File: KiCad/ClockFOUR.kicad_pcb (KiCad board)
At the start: 2 copper layers, 210 x 228 mm, 406 parts, among them P1 ICSP, P2 FTDI, P3 LDR_header, P4 Button_Header, P5 BARREL_JACK, SW1 SW_RST, U1 ATMEGA328P, U2 DS3231N, X1 CRYSTAL

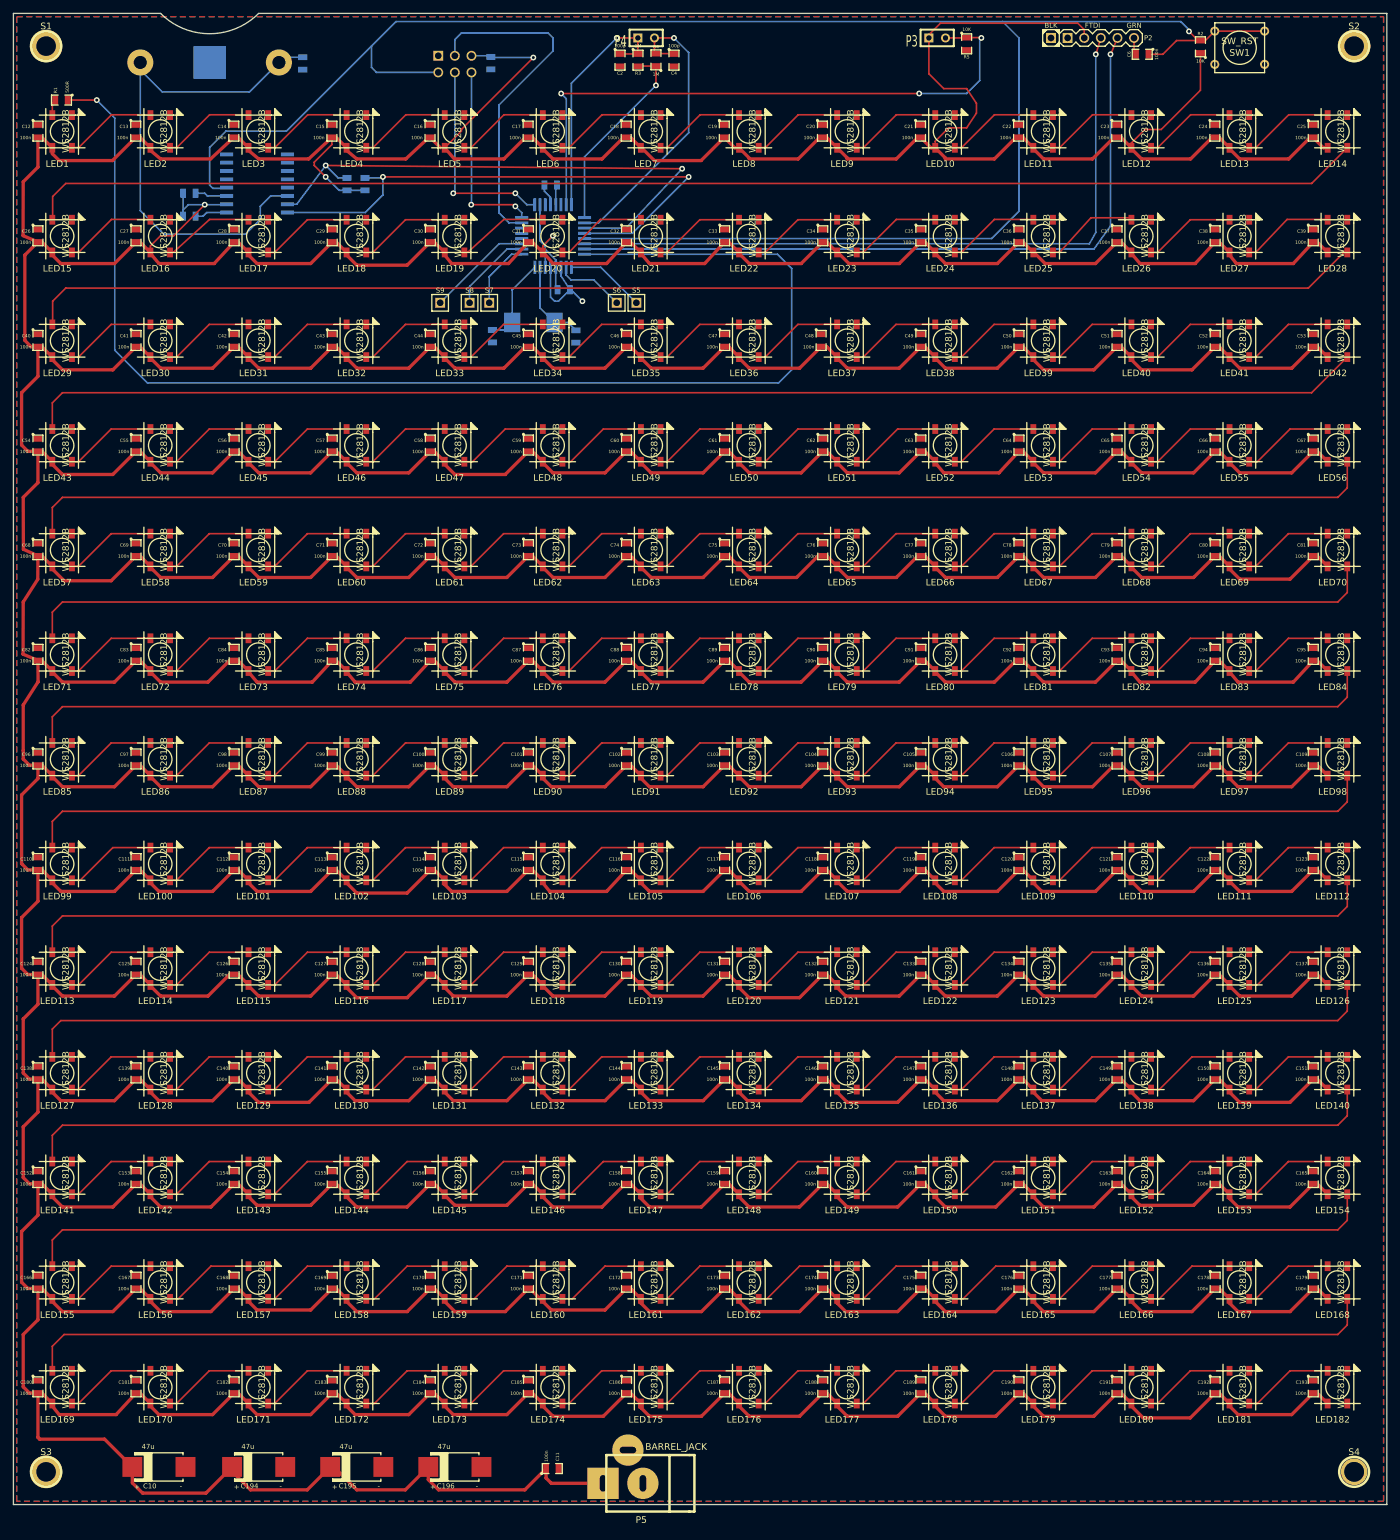
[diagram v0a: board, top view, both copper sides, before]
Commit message: Connector nudged, sent to Seed for quotation
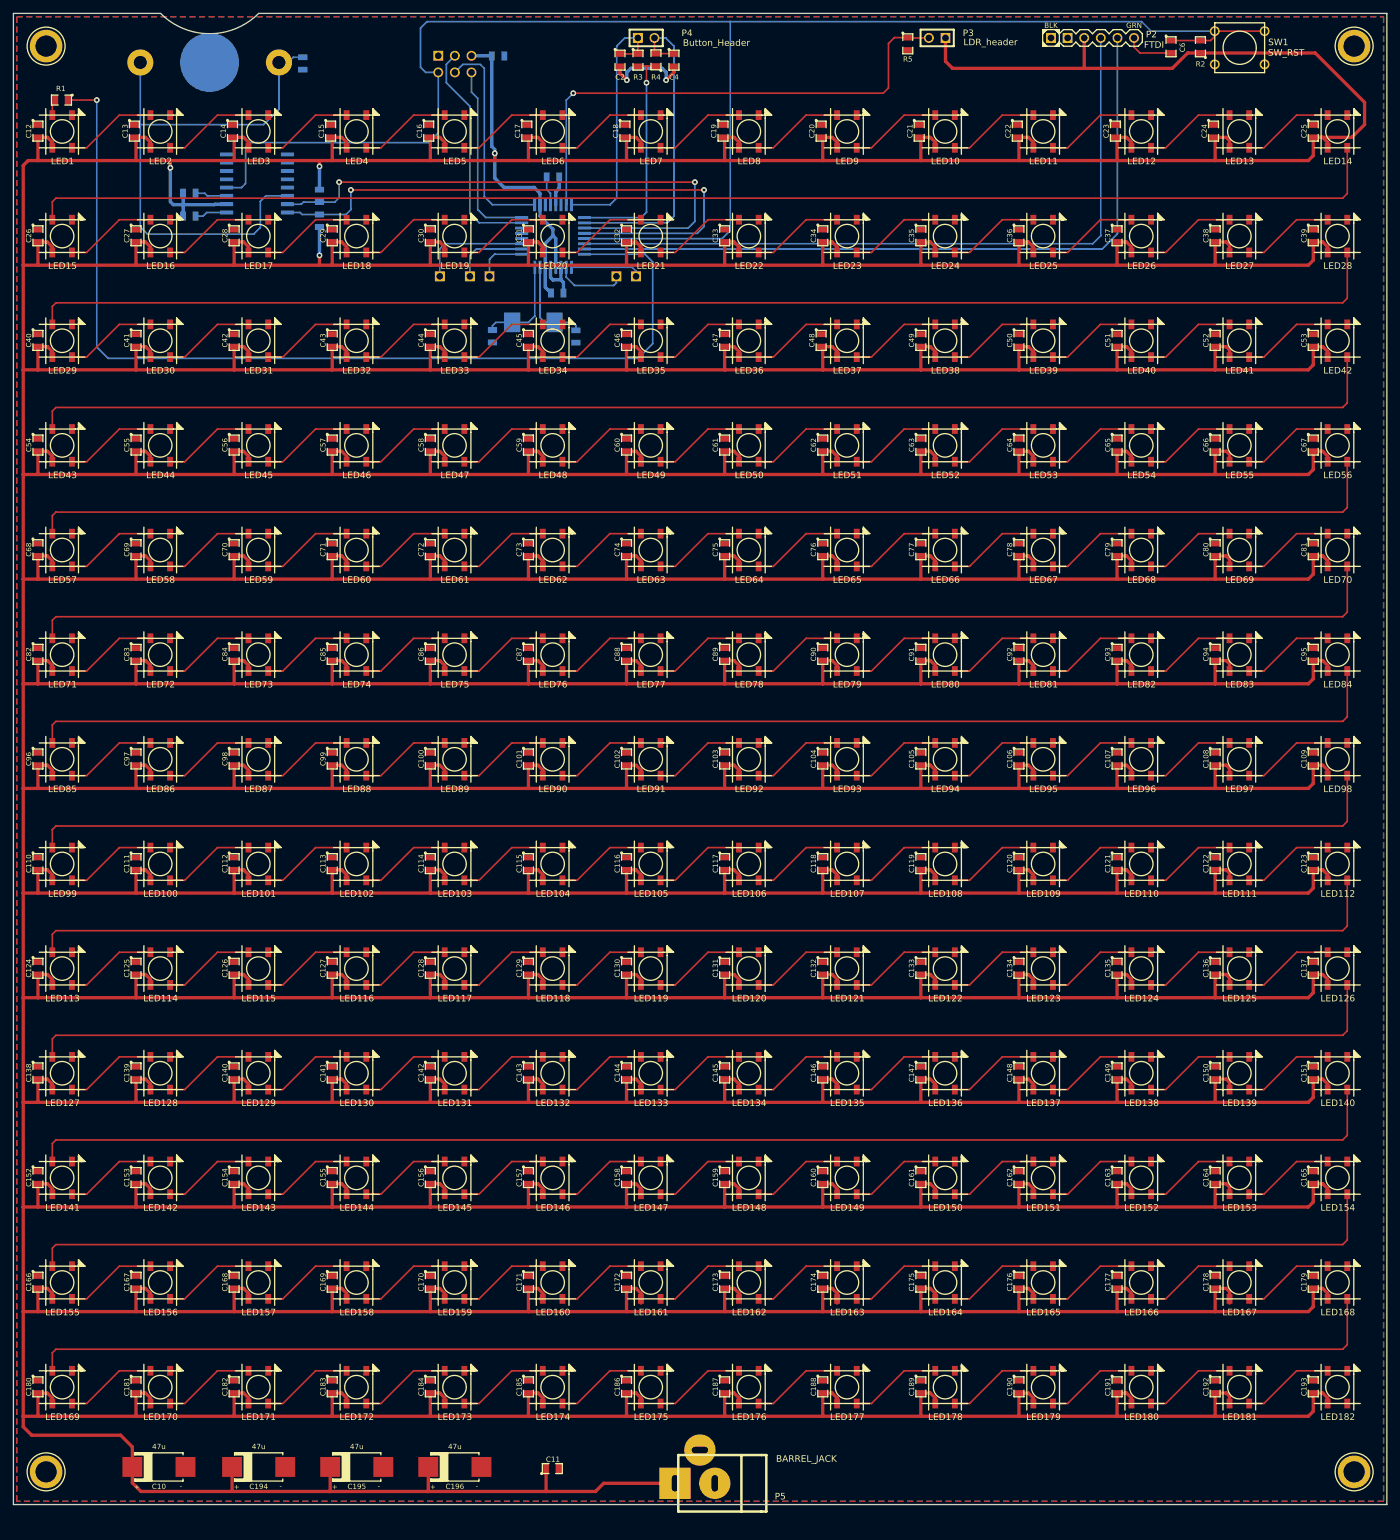
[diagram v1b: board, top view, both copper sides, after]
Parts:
- BT1: footprint CR2032 -> C4_Modules:CR2032
- C1, C11, C2, C3, C4, C5, C6, C7, C8, C9, R1, R2, R3, R4, R5, R6, R7, R8, R9: footprint SM0805 -> C4_Modules:SM0805
- C10, C194, C195, C196: footprint c_2917 -> C4_Modules:c_2917
- C100, C101, C102, C103, C104, C105, C106, C107, C108, C109, C110, C111, C112, C113, C114, C115, C116, C117, C118, C119, C12, C120, C121, C122, C123, C124, C125, C126, C127, C128, C129, C13, C130, C131, C132, C133, C134, C135, C136, C137, C138, C139, C14, C140, C141, C142, C143, C144, C145, C146, C147, C148, C149, C15, C150, C151, C152, C153, C154, C155, C156, C157, C158, C159, C16, C160, C161, C162, C163, C164, C165, C166, C167, C168, C169, C17, C170, C171, C172, C173, C174, C175, C176, C177, C178, C179, C18, C180, C181, C182, C183, C184, C185, C186, C187, C188, C189, C19, C190, C191, C192, C193, C20, C21, C22, C23, C24, C25, C26, C27, C28, C29, C30, C31, C32, C33, C34, C35, C36, C37, C38, C39, C40, C41, C42, C43, C44, C45, C46, C47, C48, C49, C50, C51, C52, C53, C54, C55, C56, C57, C58, C59, C60, C61, C62, C63, C64, C65, C66, C67, C68, C69, C70, C71, C72, C73, C74, C75, C76, C77, C78, C79, C80, C81, C82, C83, C84, C85, C86, C87, C88, C89, C90, C91, C92, C93, C94, C95, C96, C97, C98, C99: footprint C4_SM0805 -> C4_Modules:C4_SM0805
- LED1, LED10, LED100, LED101, LED102, LED103, LED104, LED105, LED106, LED107, LED108, LED109, LED11, LED110, LED111, LED112, LED113, LED114, LED115, LED116, LED117, LED118, LED119, LED12, LED120, LED121, LED122, LED123, LED124, LED125, LED126, LED127, LED128, LED129, LED13, LED130, LED131, LED132, LED133, LED134, LED135, LED136, LED137, LED138, LED139, LED14, LED140, LED141, LED142, LED143, LED144, LED145, LED146, LED147, LED148, LED149, LED15, LED150, LED151, LED152, LED153, LED154, LED155, LED156, LED157, LED158, LED159, LED16, LED160, LED161, LED162, LED163, LED164, LED165, LED166, LED167, LED168, LED169, LED17, LED170, LED171, LED172, LED173, LED174, LED175, LED176, LED177, LED178, LED179, LED18, LED180, LED181, LED182, LED19, LED2, LED20, LED21, LED22, LED23, LED24, LED25, LED26, LED27, LED28, LED29, LED3, LED30, LED31, LED32, LED33, LED34, LED35, LED36, LED37, LED38, LED39, LED4, LED40, LED41, LED42, LED43, LED44, LED45, LED46, LED47, LED48, LED49, LED5, LED50, LED51, LED52, LED53, LED54, LED55, LED56, LED57, LED58, LED59, LED6, LED60, LED61, LED62, LED63, LED64, LED65, LED66, LED67, LED68, LED69, LED7, LED70, LED71, LED72, LED73, LED74, LED75, LED76, LED77, LED78, LED79, LED8, LED80, LED81, LED82, LED83, LED84, LED85, LED86, LED87, LED88, LED89, LED9, LED90, LED91, LED92, LED93, LED94, LED95, LED96, LED97, LED98, LED99: footprint WS2812B -> C4_Modules:WS2812B
- S1, S2, S3, S4: footprint 1pin -> C4_Modules:1pin
- S5, S6, S7, S8, S9: moved to B.Cu
- moved P5 11.0 mm to (161.2, 265.8)
- moved R5 9.00 mm to (190.8, 45.8)
- moved R8 8.93 mm to (100.8, 72.6)
- moved R9 4.65 mm to (100.8, 69.0), turned to 0 degrees
- moved C6 4.62 mm to (231.0, 46.2), turned to 180 degrees
- moved S5 4.05 mm to (149.2, 81.2)
- moved S6 4.05 mm to (146.2, 81.2)
- moved S7 4.05 mm to (126.8, 81.2)
- moved S8 4.05 mm to (123.8, 81.2)
- moved S9 4.05 mm to (119.2, 81.2)
- moved C8 1.41 mm to (128.0, 47.5), turned to 270 degrees
- moved C3 1.30 mm to (136.6, 66.0)
- moved C1 1.12 mm to (137.2, 83.8)
- turned P3 to 180 degrees
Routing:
- net 5V: track 3570.5 -> 4429.9 mm
- net /RESET: track 300.6 -> 250.4 mm, vias 1 -> 0
- net /MATRIX_PIN: track 198.3 -> 152.3 mm
- net /MOSI: track 52.5 -> 34.8 mm
- net /LDR_PIN: track 94.3 -> 79.4 mm, vias 3 -> 1
- net GND: track 18.1 -> 26.4 mm, vias 1 -> 2
- net N-0000030: track 80.4 -> 87.4 mm
- net N-000005: track 2.62 -> 7.42 mm
- net /SENSE_PIN: track 30.5 -> 34.9 mm
- net /SCL: track 87.5 -> 91.4 mm
- net /Row_B/DI_B: track 204.6 -> 208.3 mm
- net /BUTTON_R: track 45.3 -> 48.9 mm, vias 1 -> 0
- net N-000002: track 13.4 -> 16.8 mm
- net /Row_C/DI_C: track 204.8 -> 208.3 mm
- net /Row_D/DI_D: track 204.9 -> 208.3 mm
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
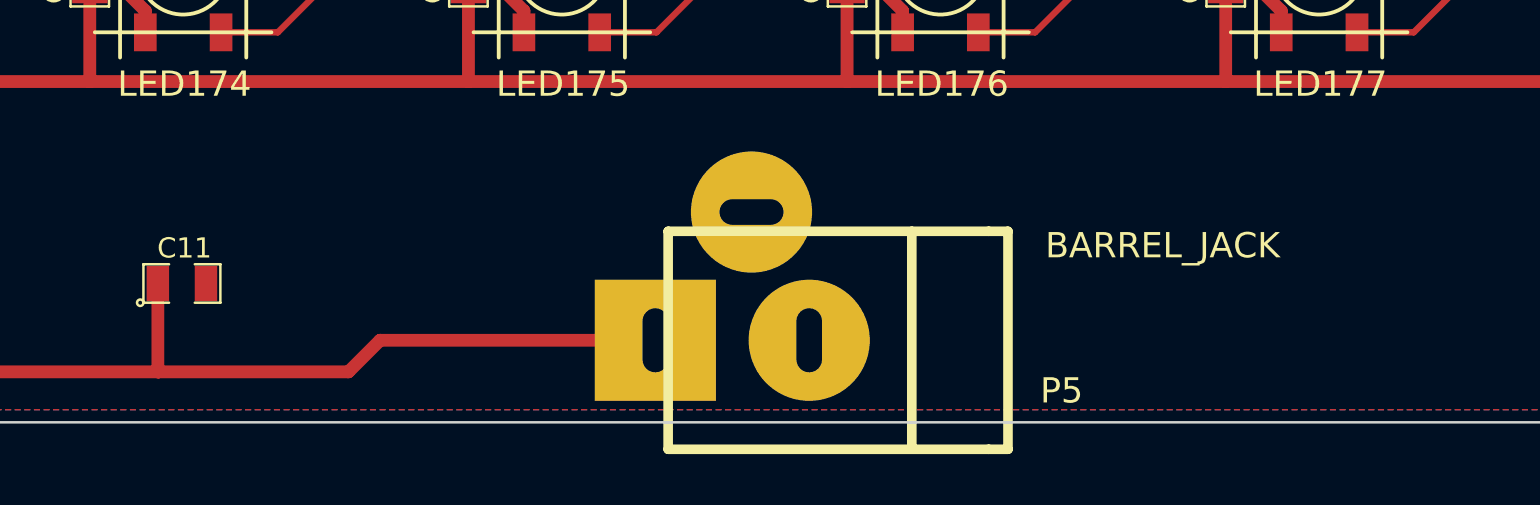
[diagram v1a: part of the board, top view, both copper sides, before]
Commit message: New power jack added
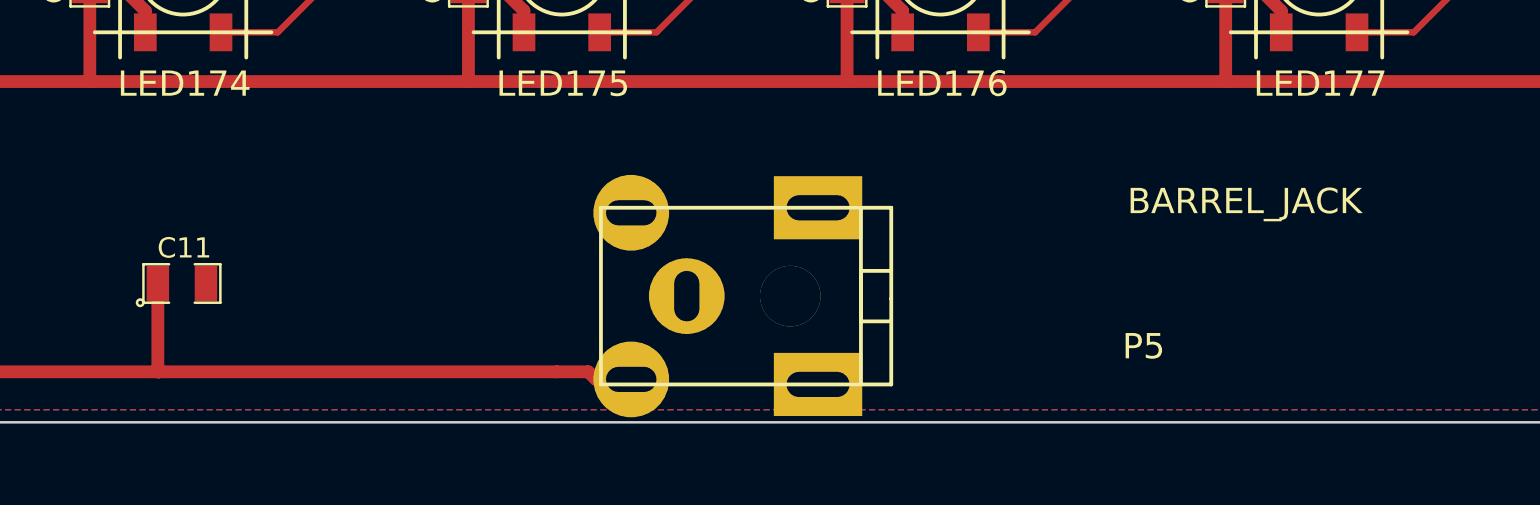
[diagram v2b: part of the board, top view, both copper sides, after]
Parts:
- P5: footprint JACK_ALIM -> JACK_PJ-047a
- moved P5 3.69 mm to (164.5, 264.0)
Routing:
- net 5V: track 4429.9 -> 4428.6 mm
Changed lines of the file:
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@@
   (general
     (links 1005)
-    (no_connects 0)
-    (area 53.899999 33.170999 264.100001 276.7)
+    (no_connects 2)
+    (area 53.949999 33.449999 264.050001 269.050001)
     (thickness 1.6)
     (drawings 131)
-    (tracks 2048)
+    (tracks 2049)
     (zones 0)
     (modules 406)
@@
     (mod_text_size 1 1)
     (mod_text_width 0.15)
-    (pad_size 1.524 1.524)
-    (pad_drill 1.016)
+    (pad_size 3 3)
+    (pad_drill 2)
     (pad_to_mask_clearance 0)
     (aux_axis_origin 54 29)
@@
     )
   )
-  (module JACK_ALIM (layer F.Cu)
-    (at 161.25 265.75 180)
-    (descr "module 1 pin (ou trou mecanique de percage)")
-    (tags "CONN JACK")
-    (fp_text reference P5 (at -10 -2 180) (layer F.SilkS)
-      (effects (font (size 1 1) (thickness 0.15)))
-    )
-    (fp_text value BARREL_JACK (at -14 3.75 180) (layer F.SilkS)
-      (effects (font (size 1 1) (thickness 0.15)))
-    )
-    (fp_line (start -7.112 -4.318) (end -7.874 -4.318) (layer F.SilkS) (width 0.381))
-    (fp_line (start -7.874 -4.318) (end -7.874 4.318) (layer F.SilkS) (width 0.381))
-    (fp_line (start -7.874 4.318) (end -7.112 4.318) (layer F.SilkS) (width 0.381))
-    (fp_line (start -4.064 -4.318) (end -4.064 4.318) (layer F.SilkS) (width 0.381))
-    (fp_line (start 5.588 -4.318) (end 5.588 4.318) (layer F.SilkS) (width 0.381))
-    (fp_line (start -7.112 4.318) (end 5.588 4.318) (layer F.SilkS) (width 0.381))
-    (fp_line (start -7.112 -4.318) (end 5.588 -4.318) (layer F.SilkS) (width 0.381))
-    (pad 2 thru_hole circle (at 0 0 180) (size 4.8006 4.8006) (drill oval 1.016 2.54)
-      (layers *.Cu *.Mask F.SilkS)
-      (net 33 GND)
-    )
-    (pad 1 thru_hole rect (at 6.096 0 180) (size 4.8006 4.8006) (drill oval 1.016 2.54)
-      (layers *.Cu *.Mask F.SilkS)
-      (net 32 5V)
-    )
-    (pad 3 thru_hole circle (at 2.286 5.08 180) (size 4.8006 4.8006) (drill oval 2.54 1.016)
-      (layers *.Cu *.Mask F.SilkS)
-      (net 33 GND)
-    )
-    (model connectors/POWER_21.wrl
-      (at (xyz 0 0 0))
-      (scale (xyz 0.8 0.8 0.8))
-      (rotate (xyz 0 0 0))
-    )
-  )
   (module PIN_ARRAY_1 (layer B.Cu)
     (at 149.2 81.2)
@@
     )
   )
+  (module JACK_PJ-047a (layer F.Cu)
+    (at 164.5 264 180)
+    (descr "module 1 pin (ou trou mecanique de percage)")
+    (tags "CONN JACK")
+    (fp_text reference P5 (at -10 -2 180) (layer F.SilkS)
+      (effects (font (size 1 1) (thickness 0.15)))
+    )
+    (fp_text value BARREL_JACK (at -14 3.75 180) (layer F.SilkS)
+      (effects (font (size 1 1) (thickness 0.15)))
+    )
+    (fp_line (start 0.1 -1) (end 1.2 -1) (layer F.SilkS) (width 0.15))
+    (fp_line (start 1.2 -1) (end 1.2 1) (layer F.SilkS) (width 0.15))
+    (fp_line (start 1.2 1) (end 0 1) (layer F.SilkS) (width 0.15))
+    (fp_line (start 1.2 -3.5) (end 1.2 3.5) (layer F.SilkS) (width 0.15))
+    (fp_line (start 0 -0.1) (end 0 -3.5) (layer F.SilkS) (width 0.15))
+    (fp_line (start 0 -3.5) (end 11.5 -3.5) (layer F.SilkS) (width 0.15))
+    (fp_line (start 11.5 -3.5) (end 11.5 3.5) (layer F.SilkS) (width 0.15))
+    (fp_line (start 11.5 3.5) (end 0 3.5) (layer F.SilkS) (width 0.15))
+    (fp_line (start 0 3.5) (end 0 -0.1) (layer F.SilkS) (width 0.15))
+    (pad 2 thru_hole circle (at 8.1 0 180) (size 3 3) (drill oval 1 2)
+      (layers *.Cu *.Mask F.SilkS)
+      (net 33 GND)
+    )
+    (pad 1 thru_hole circle (at 10.3 -3.3 180) (size 3 3) (drill oval 2 1)
+      (layers *.Cu *.Mask F.SilkS)
+      (net 32 5V)
+    )
+    (pad 3 thru_hole circle (at 10.3 3.3 180) (size 3 3) (drill oval 2 1)
+      (layers *.Cu *.Mask F.SilkS)
+      (net 33 GND)
+    )
+    (pad 4 thru_hole rect (at 2.9 -3.5 180) (size 3.5 2.5) (drill oval 2.5 1)
+      (layers *.Cu *.Mask F.SilkS)
+    )
+    (pad 5 thru_hole rect (at 2.9 3.5 180) (size 3.5 2.5) (drill oval 2.5 1)
+      (layers *.Cu *.Mask F.SilkS)
+    )
+    (pad 5 thru_hole circle (at 4 0 180) (size 2.4 2.4) (drill 2.4)
+      (layers *.Cu *.Mask F.SilkS)
+    )
+    (model connectors/POWER_21.wrl
+      (at (xyz 0 0 0))
+      (scale (xyz 0.8 0.8 0.8))
+      (rotate (xyz 0 0 0))
+    )
+  )
   (gr_line (start 76.5 41) (end 54 41) (angle 90) (layer Edge.Cuts) (width 0.1))
   (gr_line (start 91.5 41) (end 264 41) (angle 90) (layer Edge.Cuts) (width 0.1))
@@
   (segment (start 222.81 74.69) (end 222.81 44.75) (width 0.254) (layer B.Cu) (net 31) (status 20))
   (segment (start 220.47308 77.02692) (end 222.81 74.69) (width 0.254) (layer B.Cu) (net 31))
-  (segment (start 135.4475 263.5) (end 135.4475 267) (width 0.508) (layer F.Cu) (net 32))
-  (segment (start 135.4475 267) (end 143 267) (width 0.508) (layer F.Cu) (net 32))
-  (segment (start 144.25 265.75) (end 155.154 265.75) (width 0.508) (layer F.Cu) (net 32))
-  (segment (start 143 267) (end 144.25 265.75) (width 0.508) (layer F.Cu) (net 32))
+  (segment (start 135.4475 263.5) (end 135.4475 267) (width 0.508) (layer F.Cu) (net 32) (status 400000))
+  (segment (start 135.4475 267) (end 151.25 267) (width 0.508) (layer F.Cu) (net 32))
+  (segment (start 152.8 267.3) (end 154.2 267.3) (width 0.508) (layer F.Cu) (net 32) (status C00000))
+  (segment (start 152.5 267) (end 152.8 267.3) (width 0.508) (layer F.Cu) (net 32) (status 800000))
+  (segment (start 151.25 267) (end 152.5 267) (width 0.508) (layer F.Cu) (net 32))
   (segment (start 217.73 44.75) (end 217.73 49.4) (width 0.508) (layer F.Cu) (net 32) (status 10))
   (segment (start 235.5 47.0525) (end 233.5475 47.0525) (width 0.508) (layer F.Cu) (net 32) (status 10))
@@
   (segment (start 125.2 253.55) (end 122.95 253.55) (width 0.254) (layer F.Cu) (net 157) (status 20))
   (segment (start 130.2 248.55) (end 125.2 253.55) (width 0.254) (layer F.Cu) (net 157))
+  (segment (start 160.2 248.55) (end 155.2 253.55) (width 0.254) (layer F.Cu) (net 158))
   (segment (start 164.95 248.55) (end 160.2 248.55) (width 0.254) (layer F.Cu) (net 158) (status 10))
   (segment (start 155.2 253.55) (end 152.95 253.55) (width 0.254) (layer F.Cu) (net 158) (status 20))
-  (segment (start 160.2 248.55) (end 155.2 253.55) (width 0.254) (layer F.Cu) (net 158))
   (segment (start 136.7385 88.25) (end 139.5 88.25) (width 0.254) (layer B.Cu) (net 159) (status 10))
   (segment (start 140 88.75) (end 140 89.4475) (width 0.254) (layer B.Cu) (net 159) (status 20))
